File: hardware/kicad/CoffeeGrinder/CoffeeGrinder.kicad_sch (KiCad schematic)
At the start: 11 parts, among them U1 ESP32-DevKitC

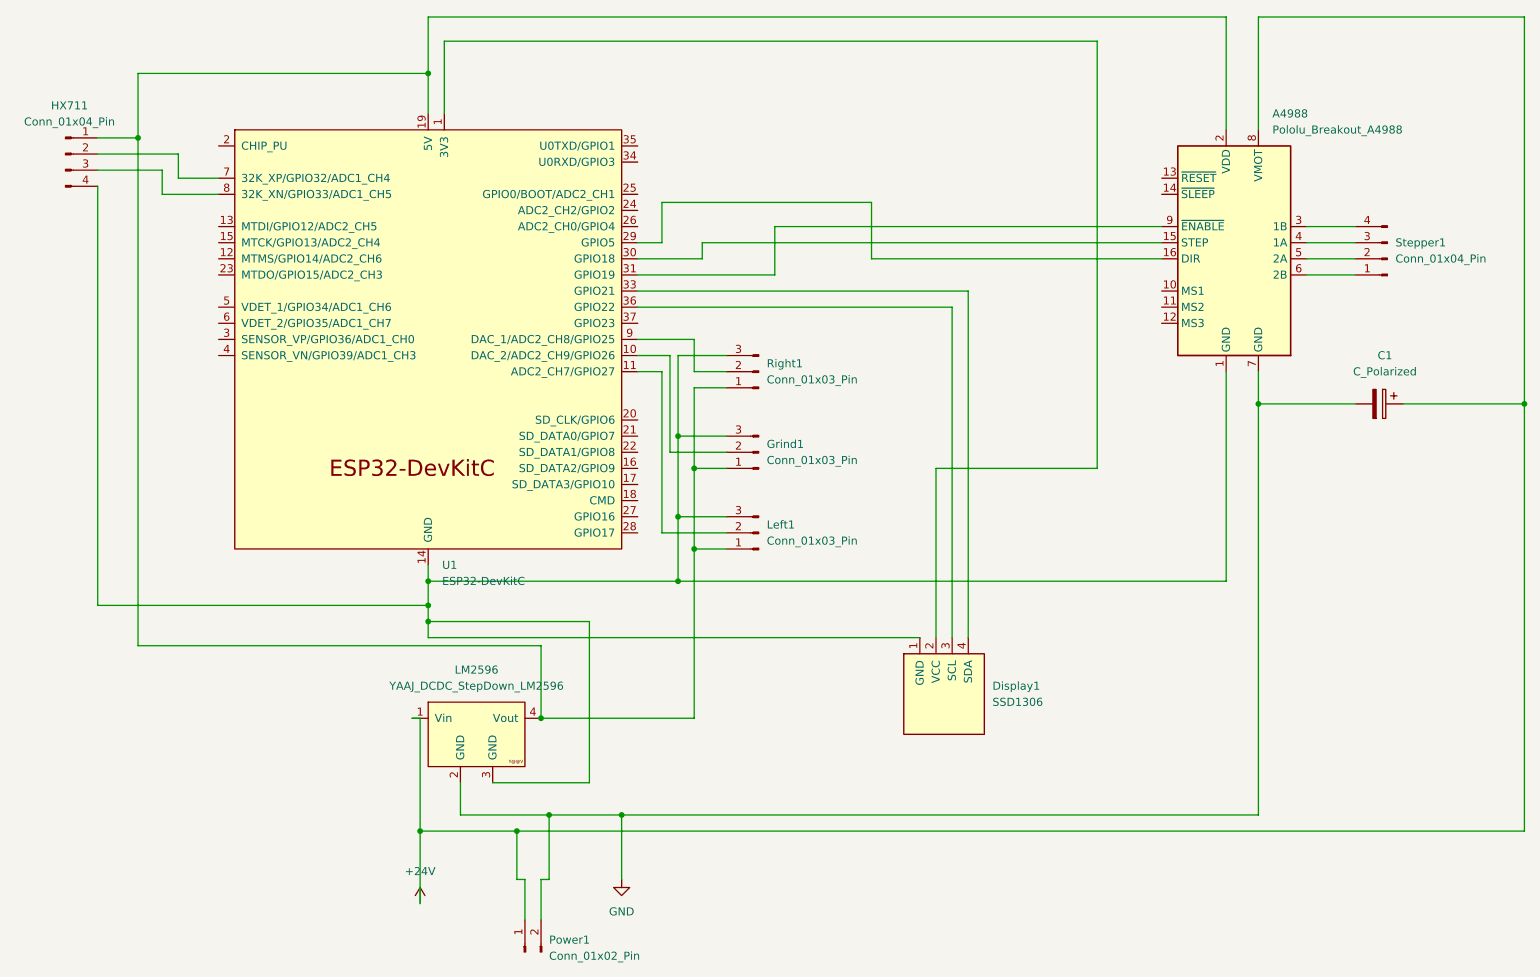
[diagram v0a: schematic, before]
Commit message: Replace stepper motor with 5010 brushless motor 360KV
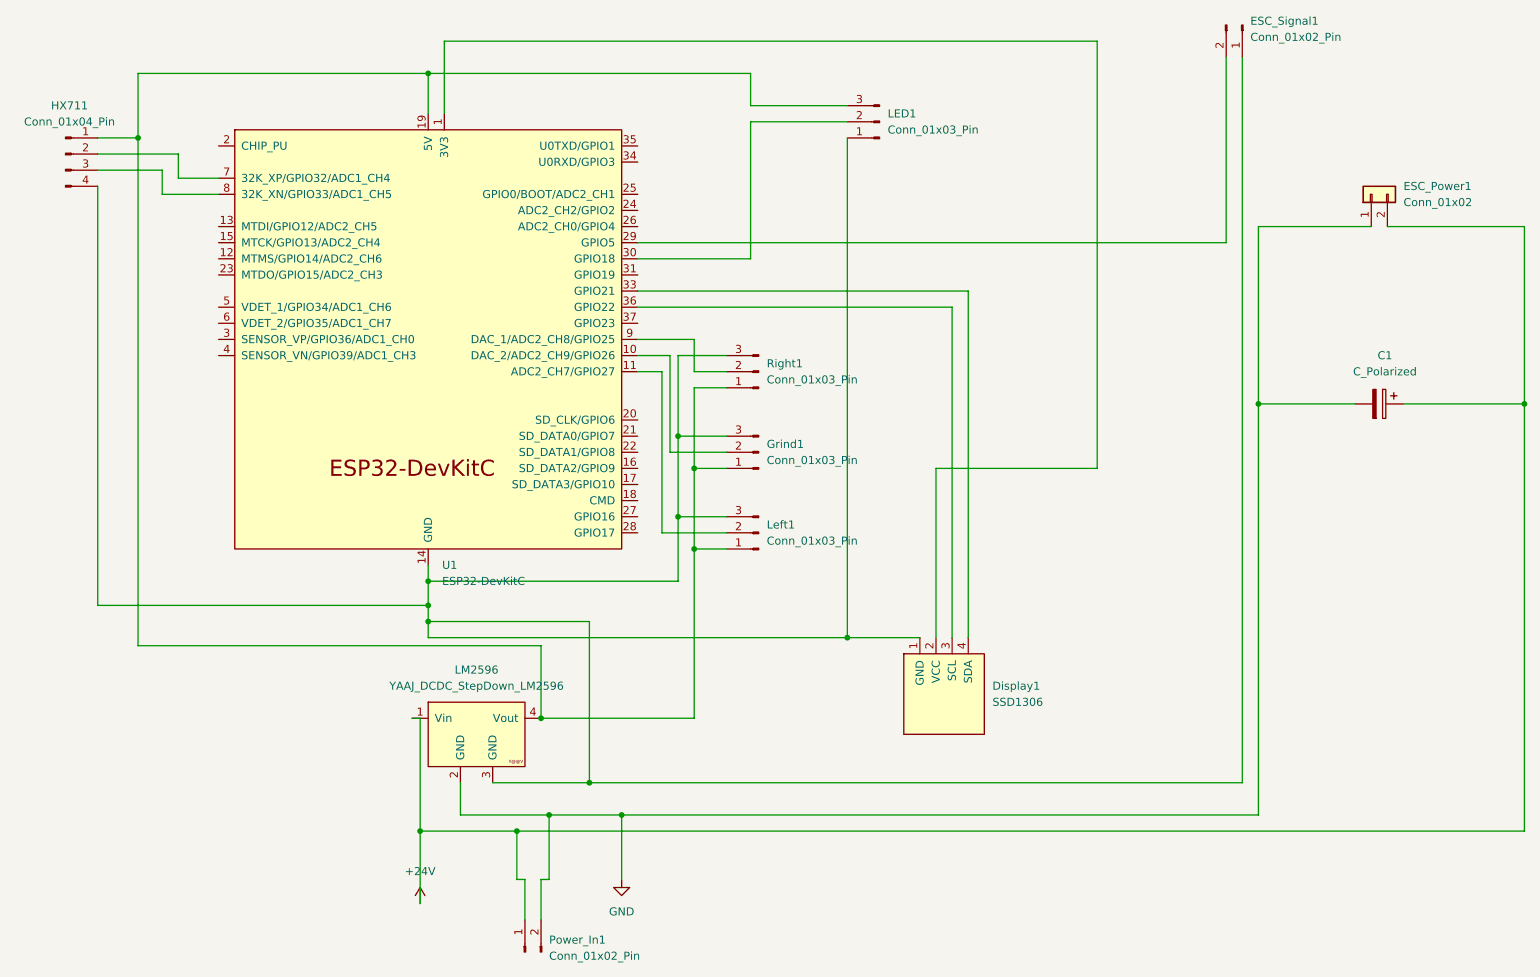
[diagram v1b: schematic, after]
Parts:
- removed A4988: Pololu_Breakout_A4988, Module:Pololu_Breakout-16_15.2x20.3mm, symbol Driver_Motor:Pololu_Breakout_A4988
- removed Stepper1: Conn_01x04_Pin, Connector_JST:JST_PH_B4B-PH-K_1x04_P2.00mm_Vertical, symbol Connector:Conn_01x04_Pin
- added ESC_Power1: Conn_01x02, Connector_AMASS:AMASS_XT30UPB-F_1x02_P5.0mm_Vertical, symbol Connector_Generic:Conn_01x02
- added ESC_Signal1: Conn_01x02_Pin, Connector_JST:JST_PH_B2B-PH-K_1x02_P2.00mm_Vertical, symbol Connector:Conn_01x02_Pin
- added LED1: Conn_01x03_Pin, Connector_JST:JST_PH_B3B-PH-K_1x03_P2.00mm_Vertical, symbol Connector:Conn_01x03_Pin
- Power_In1: renamed from Power1; footprint Connector_JST:JST_PH_B2B-PH-K_1x02_P2.00mm_Vertical -> Connector_AMASS:AMASS_XT30UPB-M_1x02_P5.0mm_Vertical
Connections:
- net +24V: now also ESC_Power1.2 (Pin_2)
- net GND: now also ESC_Power1.1 (Pin_1)
- net at Display1.1 (GND), Grind1.3 (Pin_3), HX711.4 (Pin_4)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: now also ESC_Signal1.1 (Pin_1), LED1.1 (Pin_1)
- net at Grind1.1 (Pin_1), HX711.1 (Pin_1), LM2596.4 (Vout)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: now also LED1.3 (Pin_3)
- net at U1.29 (GPIO5): now also ESC_Signal1.2 (Pin_2)
- net at U1.30 (GPIO18): now also LED1.2 (Pin_2)
